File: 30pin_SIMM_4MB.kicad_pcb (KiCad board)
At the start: 2 copper layers, 88.9 x 20 mm, 7 parts, among them IC1 4Mx4bit_DRAM, IC2 4Mx4bit_DRAM, IC3 4Mx1bit_DRAM, J1 30pin_SIMM_Edge

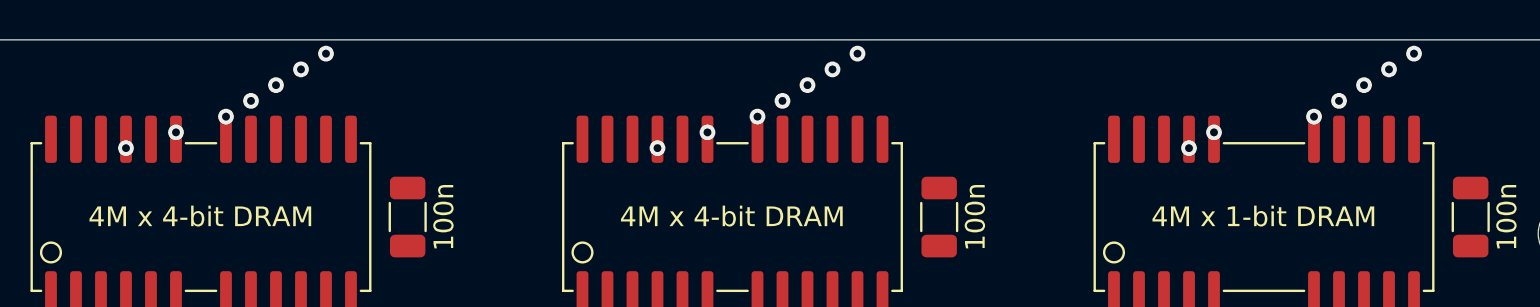
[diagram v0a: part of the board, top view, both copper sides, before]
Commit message: Closer via spacing, larger traces
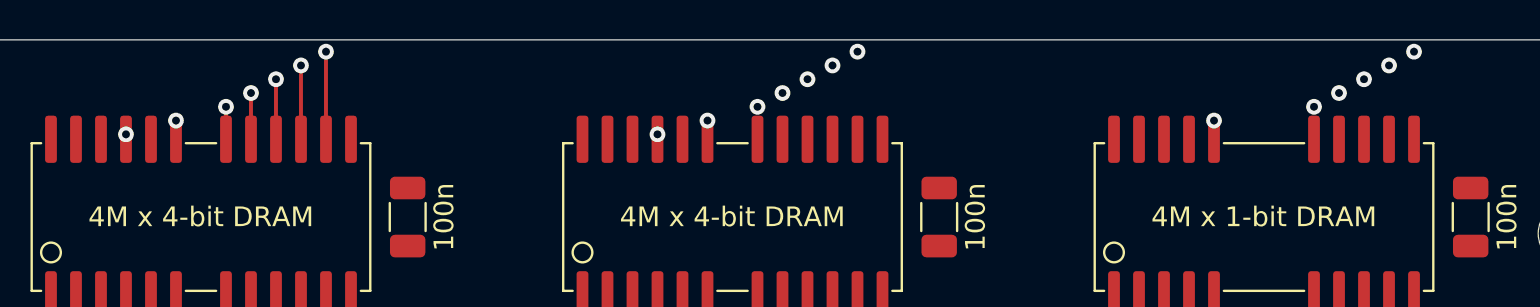
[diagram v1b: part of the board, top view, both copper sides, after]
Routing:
- net /A4: track 0.00 -> 4.70 mm
- net /A5: track 0.00 -> 4.00 mm
- net /A6: track 0.00 -> 3.30 mm
- net /A7: track 0.00 -> 2.60 mm
- net /A8: track 0.00 -> 1.90 mm
- net Net-(IC3-Pad23): vias 1 -> 0
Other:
- net class Default: trace_width 0.25 -> 0.2
- net class Small removed
- rule trace_min: 0.16 -> 0.2

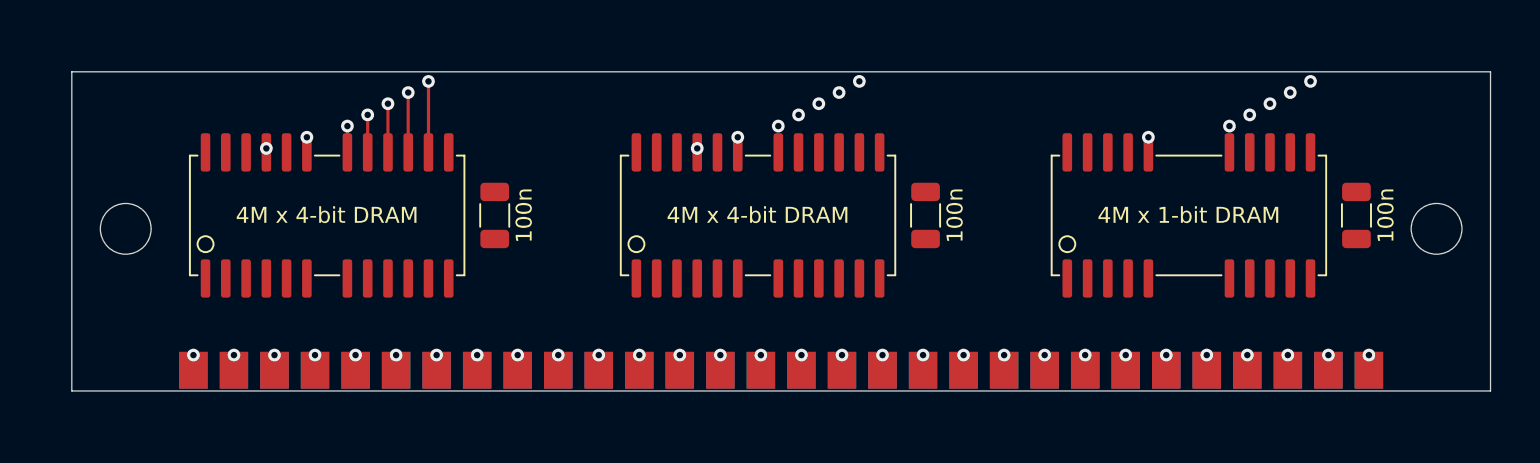
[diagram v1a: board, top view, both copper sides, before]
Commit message: Don't fear right angles
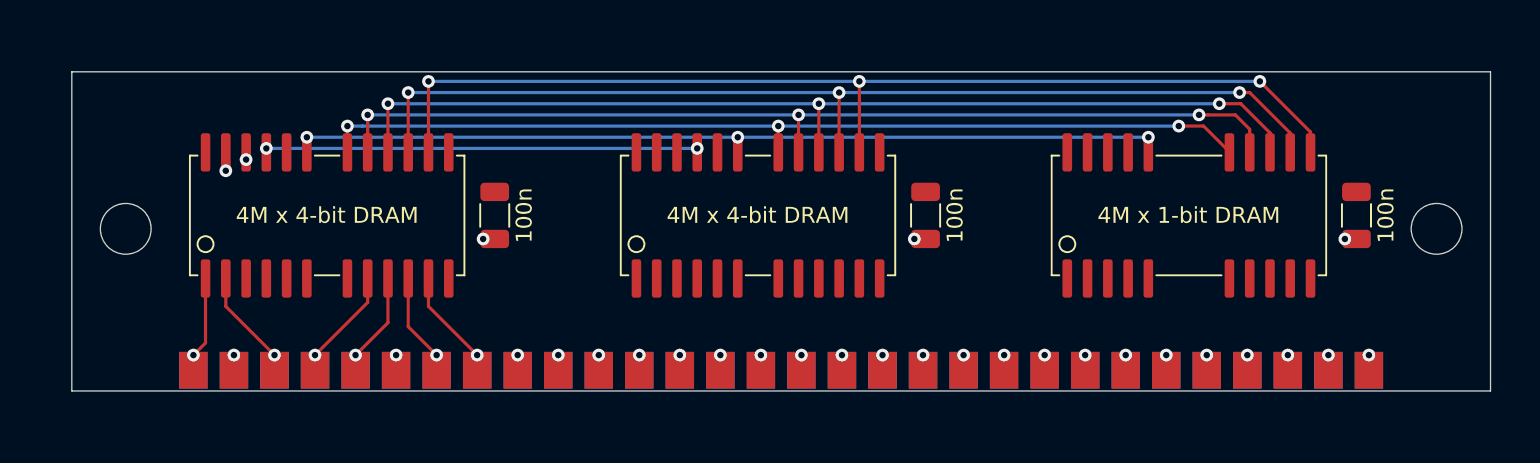
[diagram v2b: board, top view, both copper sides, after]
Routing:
- net /A4: track 4.70 -> 67.5 mm
- net /A5: track 4.00 -> 65.8 mm
- net /A6: track 3.30 -> 64.1 mm
- net /A7: track 2.60 -> 62.5 mm
- net /A8: track 1.90 -> 60.0 mm
- net /A9: track 0.00 -> 52.7 mm
- net /~CAS~: track 0.00 -> 27.1 mm
- net +5V: track 0.00 -> 9.20 mm, vias 2 -> 5
- net /A0: track 0.00 -> 6.42 mm
- net /A3: track 0.00 -> 6.31 mm
- net /DQ0: track 0.00 -> 6.31 mm
- net /A1: track 0.00 -> 5.89 mm
- net /A2: track 0.00 -> 5.79 mm
- net /DQ3: track 0.00 -> 0.32 mm, vias 1 -> 2
- net /DQ2: track 0.00 -> 0.32 mm, vias 1 -> 2

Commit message: Vias for bottom pads
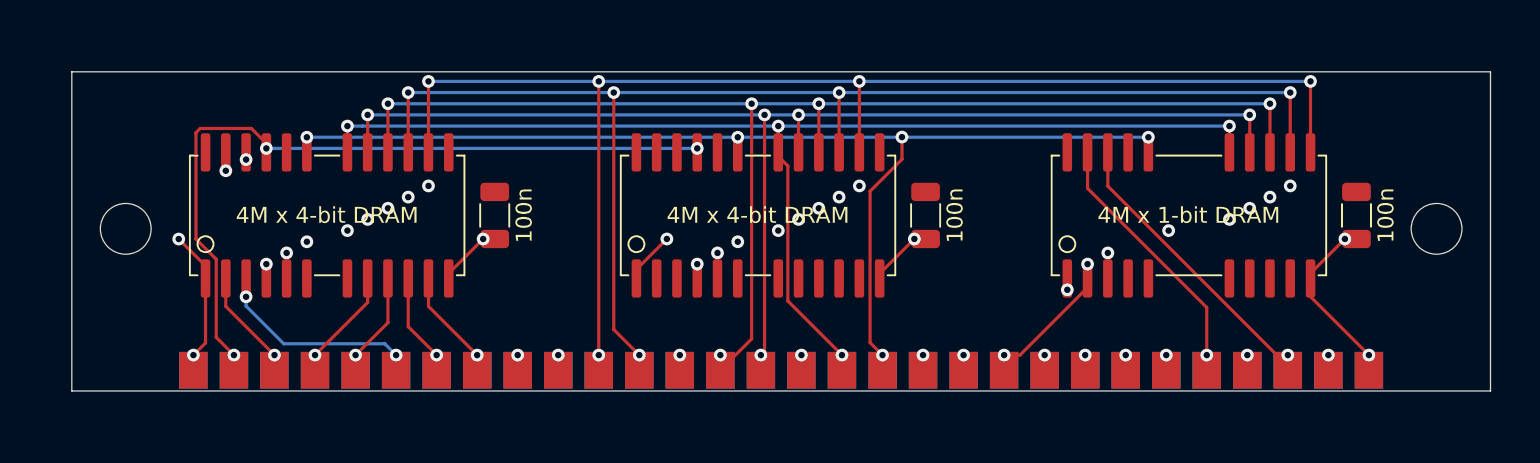
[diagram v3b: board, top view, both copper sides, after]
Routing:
- net /~CAS~: track 27.1 -> 47.8 mm
- net /A4: track 67.5 -> 86.5 mm, vias 4 -> 5
- net +5V: track 9.20 -> 27.9 mm, vias 5 -> 7
- net /A5: track 65.8 -> 84.4 mm, vias 4 -> 5
- net /A6: track 64.1 -> 82.7 mm, vias 4 -> 5
- net /~CASP~: track 0.00 -> 17.5 mm
- net /PQ: track 0.00 -> 16.5 mm
- net /A7: track 62.5 -> 78.2 mm, vias 4 -> 5
- net /A8: track 60.0 -> 75.1 mm
- net /A9: track 52.7 -> 67.5 mm, vias 4 -> 5
- net /DQ1: track 0.00 -> 11.3 mm, vias 1 -> 2
- net /~WE~: track 0.00 -> 7.80 mm, vias 1 -> 4
- net /~RAS~: track 0.00 -> 0.82 mm, vias 1 -> 4
- net /PD: vias 1 -> 2
- net /A3: vias 1 -> 4
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
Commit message: PCB Rev. 1.0 done
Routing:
- net +5V: track 27.9 -> 100.9 mm
- net /A10: track 0.00 -> 71.1 mm, vias 4 -> 5
- net /A3: track 6.31 -> 77.0 mm
- net /A2: track 5.79 -> 74.3 mm
- net /A1: track 5.89 -> 72.3 mm
- net /A0: track 6.42 -> 70.8 mm
- net /~RAS~: track 0.82 -> 65.1 mm, vias 4 -> 5
- net /A11: track 0.00 -> 57.4 mm, vias 3 -> 4
- net /~WE~: track 7.80 -> 59.3 mm
- net /DQ7: track 0.00 -> 41.4 mm, vias 1 -> 4
- net /DQ6: track 0.00 -> 36.5 mm, vias 1 -> 4
- net /DQ3: track 0.32 -> 36.7 mm, vias 2 -> 3
- net /DQ2: track 0.32 -> 29.9 mm, vias 2 -> 3
- net /DQ5: track 0.00 -> 21.7 mm, vias 1 -> 2
- net /PD: track 0.00 -> 18.1 mm
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- added copper zone on B.Cu, net GND
- added copper zone on F.Cu, net GND

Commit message: Minor fixes
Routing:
- net /DQ3: track 36.7 -> 36.9 mm, vias 3 -> 2
- net GND: vias 14 -> 17
- net /DQ2: vias 3 -> 2
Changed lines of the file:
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@@
     (thickness 1.6)
     (drawings 6)
-    (tracks 311)
+    (tracks 312)
     (zones 0)
     (modules 7)
@@
   (segment (start 109.65 92.7) (end 109.65 94.7) (width 0.2) (layer F.Cu) (net 12))
   (via (at 138.1 97.75) (size 0.8) (drill 0.4) (layers F.Cu B.Cu) (net 13))
-  (via (at 109.65 86.2) (size 0.8) (drill 0.4) (layers F.Cu B.Cu) (net 13))
   (via (at 130.48 97.75) (size 0.8) (drill 0.4) (layers F.Cu B.Cu) (net 14))
-  (via (at 110.92 85.5) (size 0.8) (drill 0.4) (layers F.Cu B.Cu) (net 14))
   (segment (start 110.92 85.3) (end 110.92 85.616412) (width 0.2) (layer F.Cu) (net 14))
   (via (at 110.16 97.75) (size 0.8) (drill 0.4) (layers F.Cu B.Cu) (net 15))
@@
   (segment (start 134.68 94.33) (end 138.1 97.75) (width 0.2) (layer B.Cu) (net 13))
   (segment (start 115.56 94.33) (end 134.68 94.33) (width 0.2) (layer B.Cu) (net 13))
-  (segment (start 109.65 85.616412) (end 109.65 85.3) (width 0.2) (layer F.Cu) (net 13))
-  (segment (start 112.563588 88.53) (end 109.65 85.616412) (width 0.2) (layer F.Cu) (net 13))
-  (segment (start 114.77 88.53) (end 112.563588 88.53) (width 0.2) (layer F.Cu) (net 13))
-  (segment (start 115.56 89.32) (end 114.77 88.53) (width 0.2) (layer F.Cu) (net 13))
-  (segment (start 115.56 94.33) (end 115.56 89.32) (width 0.2) (layer F.Cu) (net 13))
   (segment (start 110.92 85.5) (end 110.92 86.065685) (width 0.2) (layer F.Cu) (net 14))
   (segment (start 116.51 91.5283) (end 116.51 91.76) (width 0.2) (layer F.Cu) (net 14))
@@
   (via (at 157 93.78) (size 0.8) (drill 0.4) (layers F.Cu B.Cu) (net 1))
   (via (at 111 81.4) (size 0.8) (drill 0.4) (layers F.Cu B.Cu) (net 1))
+  (via (at 153.46 96.54) (size 0.8) (drill 0.4) (layers F.Cu B.Cu) (net 1))
+  (via (at 110.17 96.4) (size 0.8) (drill 0.4) (layers F.Cu B.Cu) (net 1))
+  (via (at 114.73 88.4) (size 0.8) (drill 0.4) (layers F.Cu B.Cu) (net 1))
   (segment (start 173.66 95.74) (end 173.66 97.75) (width 0.2) (layer B.Cu) (net 9))
   (segment (start 172.07 94.15) (end 173.66 95.74) (width 0.2) (layer B.Cu) (net 9))
   (segment (start 164.92 94.15) (end 172.07 94.15) (width 0.2) (layer B.Cu) (net 9))
+  (segment (start 109.65 85.3) (end 109.65 86.7) (width 0.2) (layer F.Cu) (net 13))
+  (segment (start 109.65 86.7) (end 112.24 89.29) (width 0.2) (layer F.Cu) (net 13))
+  (segment (start 114.72 89.29) (end 115.56 90.13) (width 0.2) (layer F.Cu) (net 13))
+  (segment (start 112.24 89.29) (end 114.72 89.29) (width 0.2) (layer F.Cu) (net 13))
+  (segment (start 115.56 94.33) (end 115.56 90.13) (width 0.2) (layer F.Cu) (net 13))
   (segment (start 139.953588 95.55) (end 140.46 95.55) (width 0.2) (layer F.Cu) (net 22))
   (segment (start 137.92 93.516412) (end 139.953588 95.55) (width 0.2) (layer F.Cu) (net 22))
